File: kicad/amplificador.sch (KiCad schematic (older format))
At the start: 86 parts, among them J1 Screw_Terminal_01x01, J10 Conn_01x01_Male, J11 Conn_01x01_Male, J12 Conn_01x01_Male, J13 Conn_01x01_Male, J14 Screw_Terminal_01x01, J15 Conn_01x01_Male, J16 Screw_Terminal_01x01, J17 Screw_Terminal_01x01, J18 Conn_01x01_Male, J19 Conn_01x01_Male, J2 Conn_01x01_Male, J20 Conn_01x01_Male, J21 Screw_Terminal_01x01, J22 Screw_Terminal_01x01, J23 Screw_Terminal_01x01, J24 Screw_Terminal_01x01, J3 Conn_01x01_Male, J4 Conn_01x01_Male, J5 Conn_01x01_Male, J6 Conn_01x01_Male, J7 Screw_Terminal_01x01, J8 Screw_Terminal_01x01, J9 Conn_01x01_Male, Q1 MPSA92, Q10 MPSA42, Q11 BD135, Q12 BD136, Q13 BD135, Q14 BD136, Q15 2SD1047, Q16 2SD1047, Q17 2SB817, Q18 2SB817, Q2 MPSA42, Q3 MPSA92, Q4 MPSA42, Q5 MPSA92, Q6 MPSA92, Q7 MPSA42, Q8 MPSA92, Q9 MPSA42, U1 LM385D-1.2, U2 LM385D-1.2

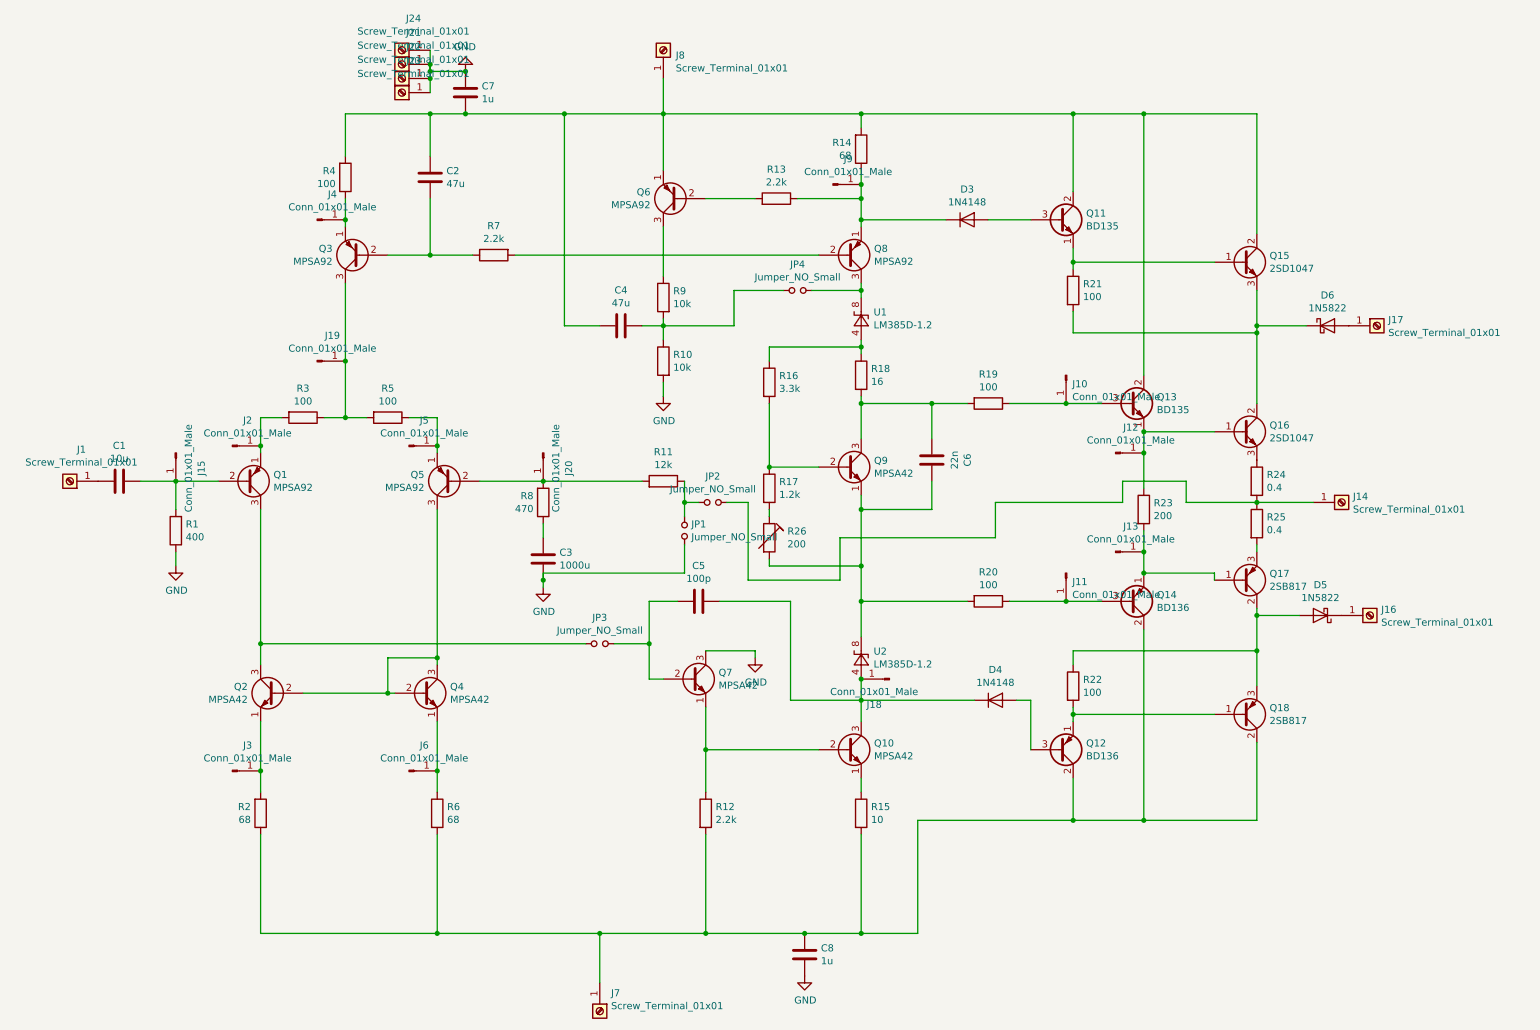
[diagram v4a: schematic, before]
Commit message: reemplazamos el q del mult del vbe x un mje, agregamos nombres a las nets e indicamos cuales son de potencia
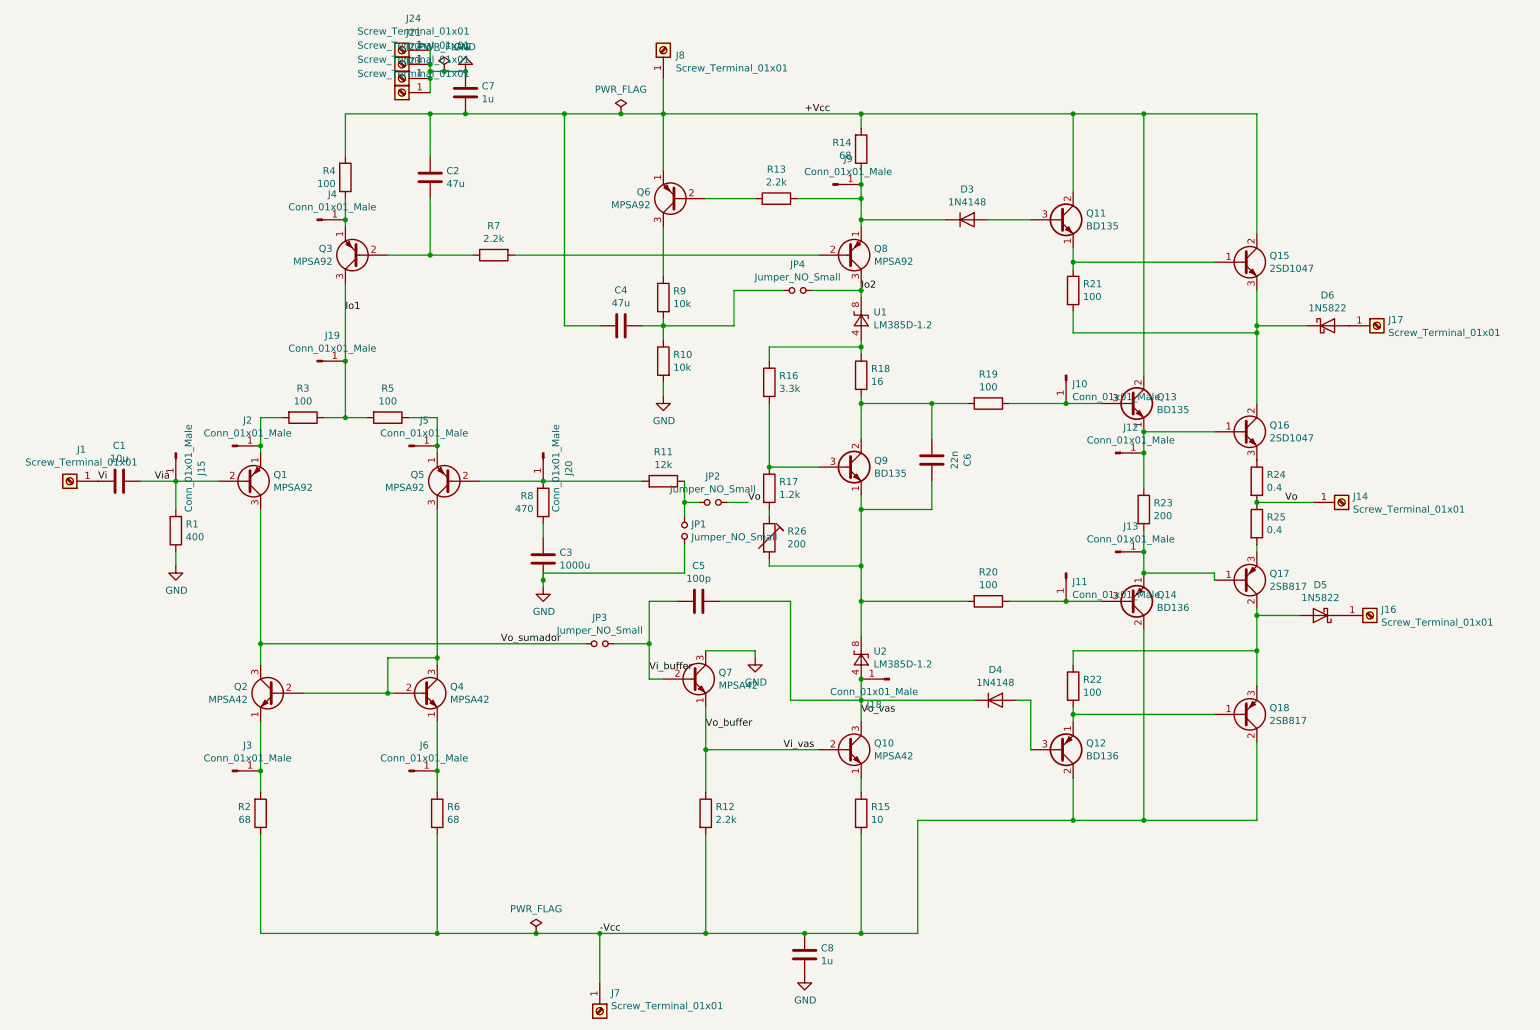
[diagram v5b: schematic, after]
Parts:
- removed Q9: MPSA42, Package_TO_SOT_THT:TO-92_Inline, symbol Transistor_BJT:MPSA42
- added Q9: BD135, Package_TO_SOT_THT:TO-126-3_Vertical, symbol Transistor_BJT:BD135
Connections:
- net Io1: now reaches J19.1 (Pin_1), Q3.3 (C), R3.1, R5.2
- net -Vcc: now reaches C8.1, J7.1 (Pin_1), Q12.2 (C), Q14.2 (C), Q18.2 (C), R12.2, R15.2, R2.1, R6.2
- net +Vcc: now reaches C2.2, C4.2, C7.2, J8.1 (Pin_1), Q11.2 (C), Q13.2 (C), Q15.2 (C), Q6.1 (E), R14.2, R4.2
- net Vi_vas: now reaches Q10.2 (B), Q7.1 (E), R12.1
- net Vo_vas: now reaches C5.1, D4.1 (K), J18.1 (Pin_1), Q10.3 (C), U2.4 (A)
- net Vi_buffer: now reaches C5.2, JP3.2, Q7.2 (B)
- net Via: now reaches C1.1, J15.1 (Pin_1), Q1.2 (B), R1.2
- net Vi: now reaches C1.2, J1.1 (Pin_1)
- net at C6.2, R18.2, R19.2: now also Q9.2 (C)
- net at R16.2, R17.1: now also Q9.3 (B)
- net at C6.1, R20.2, R26.2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: now also Q9.1 (E)
- net Vo: now reaches J14.1 (Pin_1), JP2.2, R24.2, R25.1
- net Vo_sumador: now reaches JP3.1, Q1.3 (C), Q2.3 (C)
- net Io2: now reaches JP4.2, Q8.3 (C), U1.8 (K)
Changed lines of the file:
@@
 	4600 7400 4600 7050
 Wire Wire Line
-	3450 7050 4600 7050
+	3450 7050 4150 7050
 Connection ~ 4600 7050
 Wire Wire Line
@@
 $EndComp
 $Comp
-L Transistor_BJT:MPSA42 Q9
-U 1 1 5D155344
-P 6350 3750
-F 0 "Q9" H 6541 3796 50  0000 L CNN
-F 1 "MPSA42" H 6541 3705 50  0000 L CNN
-F 2 "Package_TO_SOT_THT:TO-92_Inline" H 6550 3675 50  0001 L CIN
-F 3 "http://www.onsemi.com/pub_link/Collateral/MPSA42-D.PDF" H 6350 3750 50  0001 L CNN
-	1    6350 3750
-	1    0    0    -1
-$EndComp
-$Comp
 L Transistor_BJT:MPSA92 Q3
 U 1 1 5D155FC6
@@
 Wire Wire Line
 	5200 4000 5200 4100
-Wire Wire Line
-	8300 4000 8300 3850
-Wire Wire Line
-	8300 3850 8750 3850
-Wire Wire Line
-	8750 3850 8750 4000
-Wire Wire Line
-	8750 4000 9250 4000
 Connection ~ 9250 4000
 Wire Wire Line
@@
 Connection ~ 4350 1250
 Wire Wire Line
-	4350 1250 5050 1250
+	4350 1250 4750 1250
 Wire Wire Line
 	9250 4750 9250 4800
@@
 $EndComp
 Wire Wire Line
-	8300 4000 7400 4000
-Wire Wire Line
-	7400 4000 7400 4250
-Wire Wire Line
-	7400 4250 6300 4250
-Wire Wire Line
-	6300 4250 6300 4550
-Wire Wire Line
-	6300 4550 5650 4550
-Wire Wire Line
-	5650 4550 5650 4000
-Wire Wire Line
 	5650 4000 5500 4000
 $Comp
@@
 	3400 950  3400 900
 Wire Wire Line
-	3400 950  3650 950
+	3400 950  3500 950
 Connection ~ 3650 950
 $Comp
@@
 	3400 800  3400 900
 Connection ~ 3400 900
-Wire Wire Line
-	3400 900  3400 950
+Text Label 6050 1250 0    50   ~ 0
++Vcc
+Text Label 4600 7050 0    50   ~ 0
+-Vcc
+Text Label 9450 4000 0    50   ~ 0
+Vo
+Text Label 5650 4000 0    50   ~ 0
+Vo
+Text Label 1450 3850 0    50   ~ 0
+Via
+Text Label 1050 3850 0    50   ~ 0
+Vi
+Text Label 2800 2650 0    50   ~ 0
+Io1
+Text Label 6450 2500 0    50   ~ 0
+Io2
+Text Label 6450 5500 0    50   ~ 0
+Vo_vas
+Text Label 3900 5000 0    50   ~ 0
+Vo_sumador
+Text Label 4950 5200 0    50   ~ 0
+Vi_buffer
+Text Label 5350 5600 0    50   ~ 0
+Vo_buffer
+Text Label 5900 5750 0    50   ~ 0
+Vi_vas
+$Comp
+L power:PWR_FLAG #FLG0101
+U 1 1 5D322BEE
+P 4150 7050
+F 0 "#FLG0101" H 4150 7125 50  0001 C CNN
+F 1 "PWR_FLAG" H 4150 7223 50  0000 C CNN
+F 2 "" H 4150 7050 50  0001 C CNN
+F 3 "~" H 4150 7050 50  0001 C CNN
+	1    4150 7050
+	1    0    0    -1
+$EndComp
+Connection ~ 4150 7050
+Wire Wire Line
+	4150 7050 4600 7050
+$Comp
+L power:PWR_FLAG #FLG0102
+U 1 1 5D323768
+P 3500 950
+F 0 "#FLG0102" H 3500 1025 50  0001 C CNN
+F 1 "PWR_FLAG" H 3500 1123 50  0000 C CNN
+F 2 "" H 3500 950 50  0001 C CNN
+F 3 "~" H 3500 950 50  0001 C CNN
+	1    3500 950
+	1    0    0    -1
+$EndComp
+Connection ~ 3500 950
+Wire Wire Line
+	3500 950  3650 950
+$Comp
+L power:PWR_FLAG #FLG0103
+U 1 1 5D32478A
+P 4750 1250
+F 0 "#FLG0103" H 4750 1325 50  0001 C CNN
+F 1 "PWR_FLAG" H 4750 1423 50  0000 C CNN
+F 2 "" H 4750 1250 50  0001 C CNN
+F 3 "~" H 4750 1250 50  0001 C CNN
+	1    4750 1250
+	1    0    0    -1
+$EndComp
+Connection ~ 4750 1250
+Wire Wire Line
+	4750 1250 5050 1250
+$Comp
+L Transistor_BJT:BD135 Q9
+U 1 1 5D36A4F9
+P 6350 3750
+F 0 "Q9" H 6542 3796 50  0000 L CNN
+F 1 "BD135" H 6542 3705 50  0000 L CNN
+F 2 "Package_TO_SOT_THT:TO-126-3_Vertical" H 6550 3675 50  0001 L CIN
+F 3 "http://www.st.com/internet/com/TECHNICAL_RESOURCES/TECHNICAL_LITERATURE/DATASHEET/CD00001225.pdf" H 6350 3750 50  0001 L CNN
+	1    6350 3750
+	1    0    0    -1
+$EndComp
 $EndSCHEMATC

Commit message: actualizamos lista de materiales y algunos valores del circuito que estaban mal
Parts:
- R1: value 400 -> 12k
- R18: value 16 -> 10
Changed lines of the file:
@@
 P 1600 4200
 F 0 "R1" H 1530 4154 50  0000 R CNN
-F 1 "400" H 1530 4245 50  0000 R CNN
+F 1 "12k" H 1530 4245 50  0000 R CNN
 F 2 "Resistor_SMD:R_0805_2012Metric_Pad1.15x1.40mm_HandSolder" V 1530 4200 50  0001 C CNN
 F 3 "~" H 1600 4200 50  0001 C CNN
@@
 P 6450 3100
 F 0 "R18" H 6520 3146 50  0000 L CNN
-F 1 "16" H 6520 3055 50  0000 L CNN
+F 1 "10" H 6520 3055 50  0000 L CNN
 F 2 "Resistor_SMD:R_0805_2012Metric_Pad1.15x1.40mm_HandSolder" V 6380 3100 50  0001 C CNN
 F 3 "~" H 6450 3100 50  0001 C CNN

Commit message: el jumper JP4 estaba mal, tenía que ir a tierra, se actualizó el esquemático y el pcb. En el pcb se saco una via
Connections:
- net GND: now also JP4.1
- net at C4.1, R10.1, R9.2: no longer JP4.1
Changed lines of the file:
@@
 Wire Wire Line
 	5900 2500 5550 2500
-Wire Wire Line
-	5550 2500 5550 2750
-Wire Wire Line
-	5550 2750 5050 2750
 $Comp
 L Connector:Conn_01x01_Male J19
@@
 	1    0    0    -1
 $EndComp
+Wire Wire Line
+	5550 2500 5550 3250
+Wire Wire Line
+	5550 3250 5050 3250
+Connection ~ 5050 3250
 $EndSCHEMATC

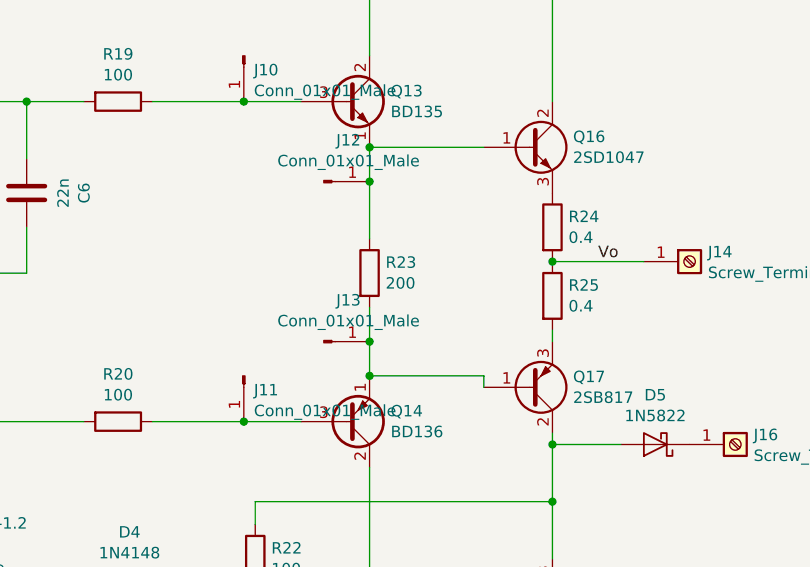
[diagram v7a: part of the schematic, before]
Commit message: cambiamos resistencia de 200 por una de 220
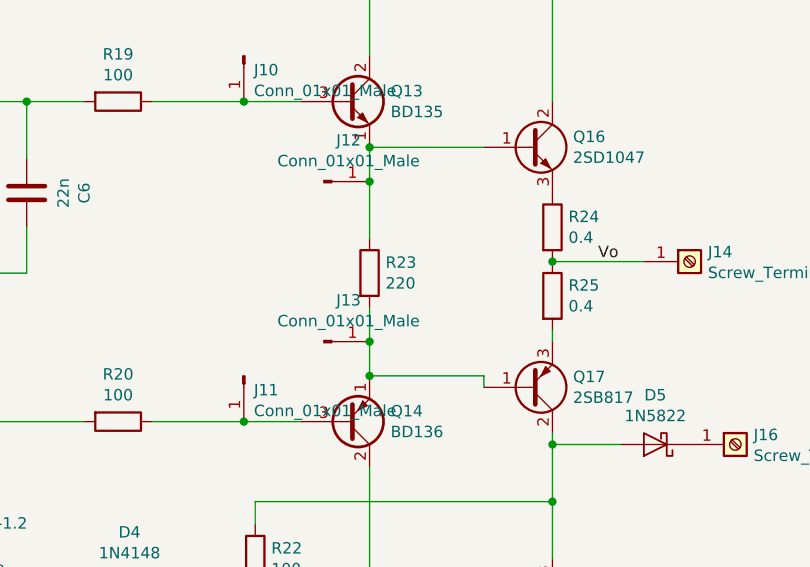
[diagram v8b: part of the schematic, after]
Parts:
- R23: value 200 -> 220
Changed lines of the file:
@@
 P 8450 4050
 F 0 "R23" H 8520 4096 50  0000 L CNN
-F 1 "200" H 8520 4005 50  0000 L CNN
+F 1 "220" H 8520 4005 50  0000 L CNN
 F 2 "Resistor_SMD:R_0805_2012Metric_Pad1.15x1.40mm_HandSolder" V 8380 4050 50  0001 C CNN
 F 3 "~" H 8450 4050 50  0001 C CNN
